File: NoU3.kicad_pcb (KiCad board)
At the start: 4 copper layers, 46 x 56 mm, 126 parts, among them J1 JST SR/SZ, J10 JST SR/SZ, J11 Screw_Terminal_01x02, J12 Screw_Terminal_01x02, J13 JST SR/SZ, J14 RFANT3216120A5T, J15 Barrel_Jack, J16 VIN, J17 JST SR/SZ, J18 GND, J2 Screw_Terminal_01x02, J3 Screw_Terminal_01x02, J4 JST SR/SZ, J5 Screw_Terminal_01x02, J6 Screw_Terminal_01x02, J7 JST SR/SZ, J8 Screw_Terminal_01x02, J9 Screw_Terminal_01x02, Q1 AO3401A, SW1 reset, SW2 boot, T1 Tab, U1 HR8833, U10 PCA9685BS, U11 Qwiic1, U15 SY8113BADC, U16 SY8113BADC, U17 USB_C_Receptacle, U18 ServoPorts_2x3, U19 ServoPorts_2x3, U2 ESP32-S3FN8, U25 MMC5983MA, U26 LSM6DSO, U3 Crystal_ESP32, U4 HR8833, U5 HR8833, U6 HR8833, U7 ServoPorts_2x3, U8 5.8 ZSPT, U9 USBLC6-2P6

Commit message: first commit for V3.4 changes
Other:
- board text added: "Alfredo NoU V3.4"
- board text removed: "Alfredo NoU V3.3"
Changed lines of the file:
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@@
 		(layer "F.SilkS")
+	)
+	(gr_line
+		(start 2.6 21.94)
+		(end 2.6 15.14)
+		(stroke
+			(width 0.25)
+			(type default)
+		)
+		(layer "F.SilkS")
+	)
+	(gr_circle
+		(center -6 5)
+		(end -9.048 5)
+		(stroke
+			(width 0.254)
+			(type solid)
+		)
+		(fill no)
+		(locked yes)
+		(layer "F.SilkS")
+	)
+	(gr_line
+		(start 8 18.6)
+		(end 3.8 18.6)
+		(stroke
+			(width 0.8)
+			(type default)
+		)
+		(layer "B.SilkS")
+	)
+	(gr_line
+		(start 8.5 18.1)
+		(end 8 18.6)
+		(stroke
+			(width 0.8)
+			(type default)
+		)
+		(layer "B.SilkS")
+	)
+	(gr_line
+		(start 9.2 18.1)
+		(end 8.5 18.1)
+		(stroke
+			(width 0.8)
+			(type default)
+		)
+		(layer "B.SilkS")
 	)
 	(gr_poly
@@
 		(fill no)
 		(locked yes)
-		(layer "F.SilkS")
-	)
-	(gr_line
-		(start 2.6 21.94)
-		(end 2.6 15.14)
-		(stroke
-			(width 0.25)
-			(type default)
-		)
-		(layer "F.SilkS")
-	)
-	(gr_circle
-		(center -6 5)
-		(end -9.048 5)
-		(stroke
-			(width 0.254)
-			(type solid)
-		)
-		(fill no)
-		(locked yes)
-		(layer "F.SilkS")
-	)
-	(gr_line
-		(start 8 18.6)
-		(end 3.8 18.6)
-		(stroke
-			(width 0.8)
-			(type default)
-		)
-		(layer "B.SilkS")
-	)
-	(gr_line
-		(start 8.5 18.1)
-		(end 8 18.6)
-		(stroke
-			(width 0.8)
-			(type default)
-		)
-		(layer "B.SilkS")
-	)
-	(gr_line
-		(start 9.2 18.1)
-		(end 8.5 18.1)
-		(stroke
-			(width 0.8)
-			(type default)
-		)
-		(layer "B.SilkS")
+		(layer "Dwgs.User")
 	)
 	(gr_arc
@@
 		)
 	)
-	(gr_text "Alfredo NoU V3.3"
+	(gr_text "Alfredo NoU V3.4"
 		(at -6.6 28.1 180)
 		(layer "B.SilkS")

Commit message: bumped version to NoU3.5
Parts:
- removed T1 (x4): Tab, PCM_kikit:Tab
- R29: value 3K -> 1K
- R30: value 1K -> 6K8
- U26: value LSM6DSO -> LSM6DSDTR
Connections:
- TP4 pad 1: Net-(U10-EXTCLK) -> M_ECLK
- U10 pad 18: /MotorSystem/MotorDriver-4/AIN1 -> /MotorSystem/MotorDriver-4/AIN2
- U10 pad 22: Net-(U10-EXTCLK) -> M_ECLK
- U2 pad 18: unconnected-(U2-GPIO13-Pad18) -> M_ECLK
- U6 pad 15: /MotorSystem/MotorDriver-4/AIN1 -> /MotorSystem/MotorDriver-4/AIN2
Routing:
- net M_ECLK: track 0.00 -> 25.7 mm, vias 0 -> 2
- net /MotorSystem/MotorDriver-4/AIN2: track 0.00 -> 7.70 mm, vias 0 -> 2
- net /MotorSystem/MotorDriver-4/AIN1: track 16.2 -> 8.55 mm, vias 4 -> 2
- net GND: track 148.8 -> 153.7 mm
- net +3V3: track 80.3 -> 83.5 mm
- net Net-(U10-EXTCLK): track 3.19 -> 0.00 mm, vias 1 -> 0
- net M_OE: track 34.6 -> 34.4 mm, vias 2 -> 3
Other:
- outline, holes or cut-outs redrawn
- board text added: "Alfredo NoU V3.5"
- board text removed: "Alfredo NoU V3.4"

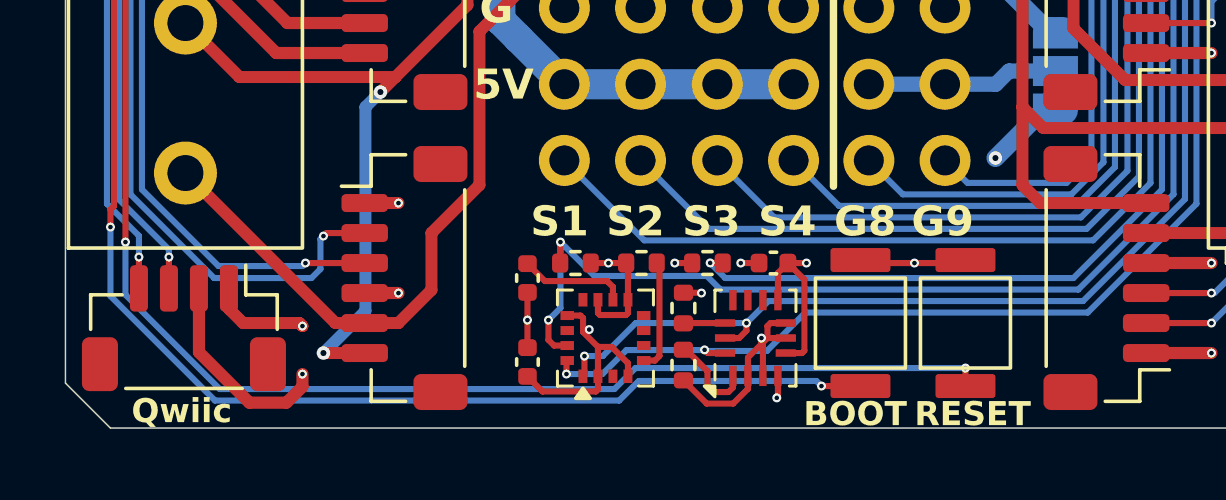
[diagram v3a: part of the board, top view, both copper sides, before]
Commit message: removed mag sensor, improved regulator resistor values
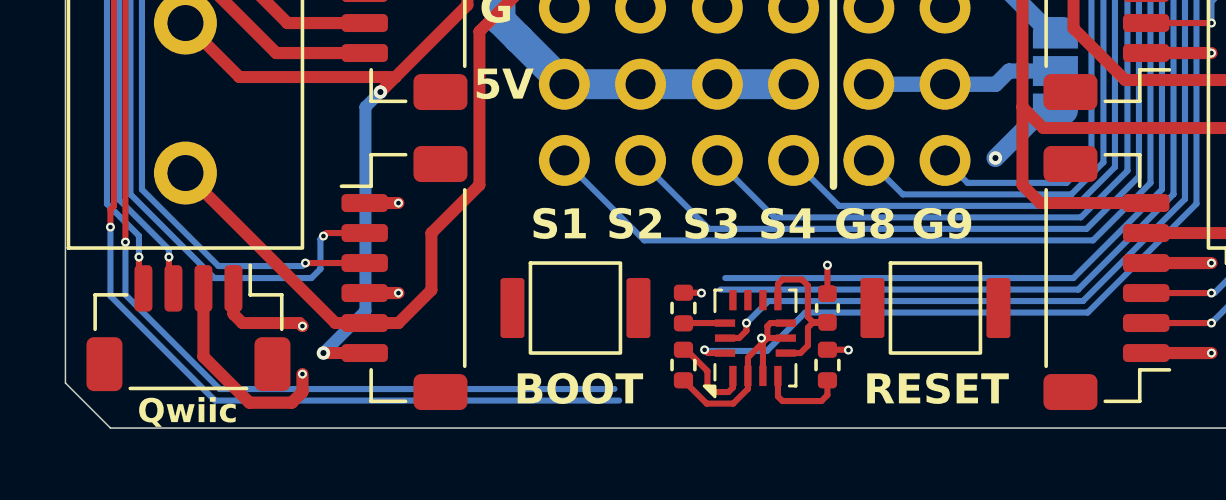
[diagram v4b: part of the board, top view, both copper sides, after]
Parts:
- removed C42: 100nF, Capacitor_SMD:C_0402_1005Metric
- removed C43: 10uF, Capacitor_SMD:C_0402_1005Metric
- removed R25, R28: 10K, Resistor_SMD:R_0402_1005Metric
- removed U25: MMC5983MA, Package_LGA:LGA-16_3x3mm_P0.5mm
- R29: value 1K -> 3K
- R30: value 6K8 -> 5K
- moved SW2 9.51 mm to (-6.00, 26.0), turned to 0 degrees
- moved R24 5.25 mm to (2.40, 27.9), turned to 90 degrees
- moved C40 2.34 mm to (2.40, 26.0), turned to 90 degrees
- moved SW1 1.12 mm to (6.00, 26.0), turned to 0 degrees
- moved U11 0.15 mm to (-18.9, 26.7)
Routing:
- net Net-(U2-CHIP_PU): track 107.5 -> 94.9 mm, vias 4 -> 3
- net SF_INT1: track 58.4 -> 47.6 mm, vias 3 -> 1
- net GND: track 153.7 -> 144.5 mm, vias 58 -> 55
- net Net-(U2-GPIO0): track 104.4 -> 96.0 mm, vias 4 -> 3
- net +3V3: track 83.5 -> 75.9 mm, vias 24 -> 22
- net SF_SCL: track 68.3 -> 61.8 mm, vias 5 -> 4
- net SF_SDA: track 72.0 -> 66.6 mm, vias 5 -> 4
- net SF_INT2: track 54.1 -> 49.8 mm, vias 3 -> 1
- net Net-(U25-SPI_SDO): track 3.72 -> 0.00 mm
- net Net-(U25-CAP): track 3.60 -> 0.00 mm

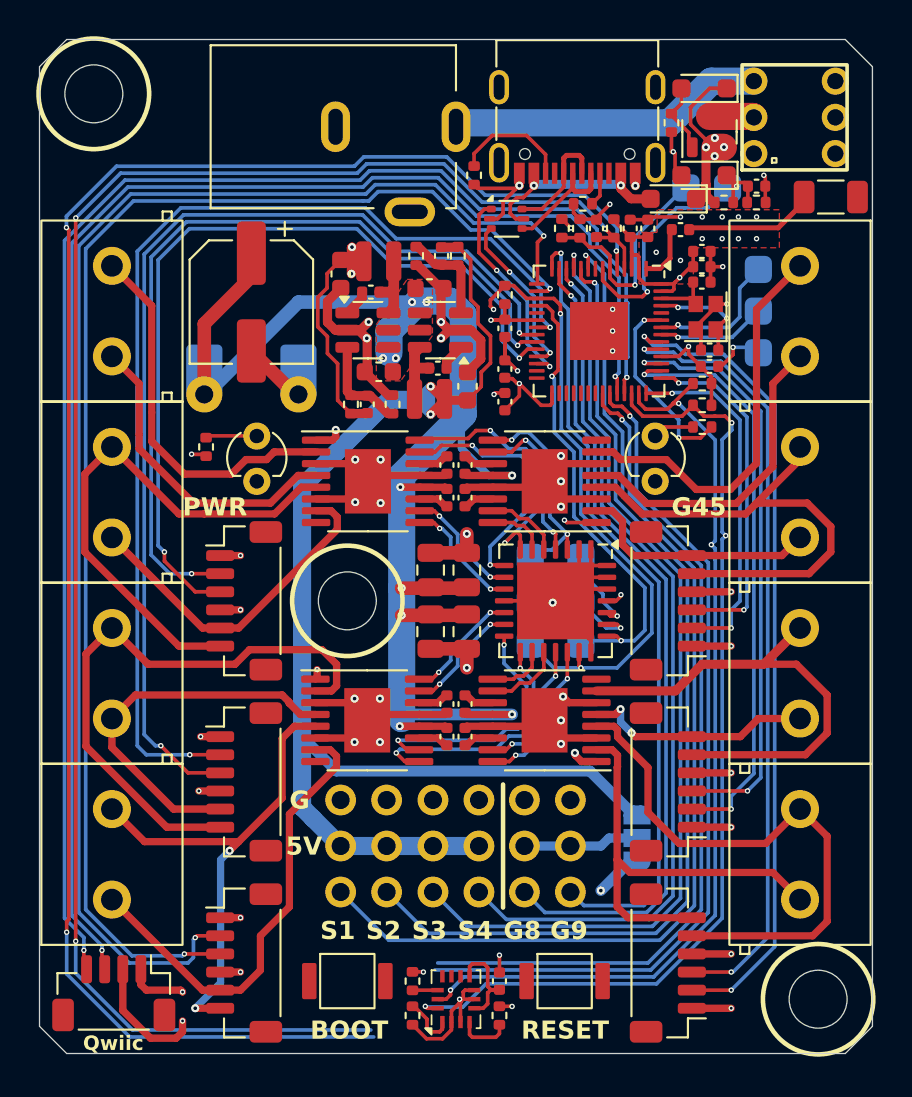
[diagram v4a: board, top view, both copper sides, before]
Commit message: added 7th encoder, 2nd 220uf cap
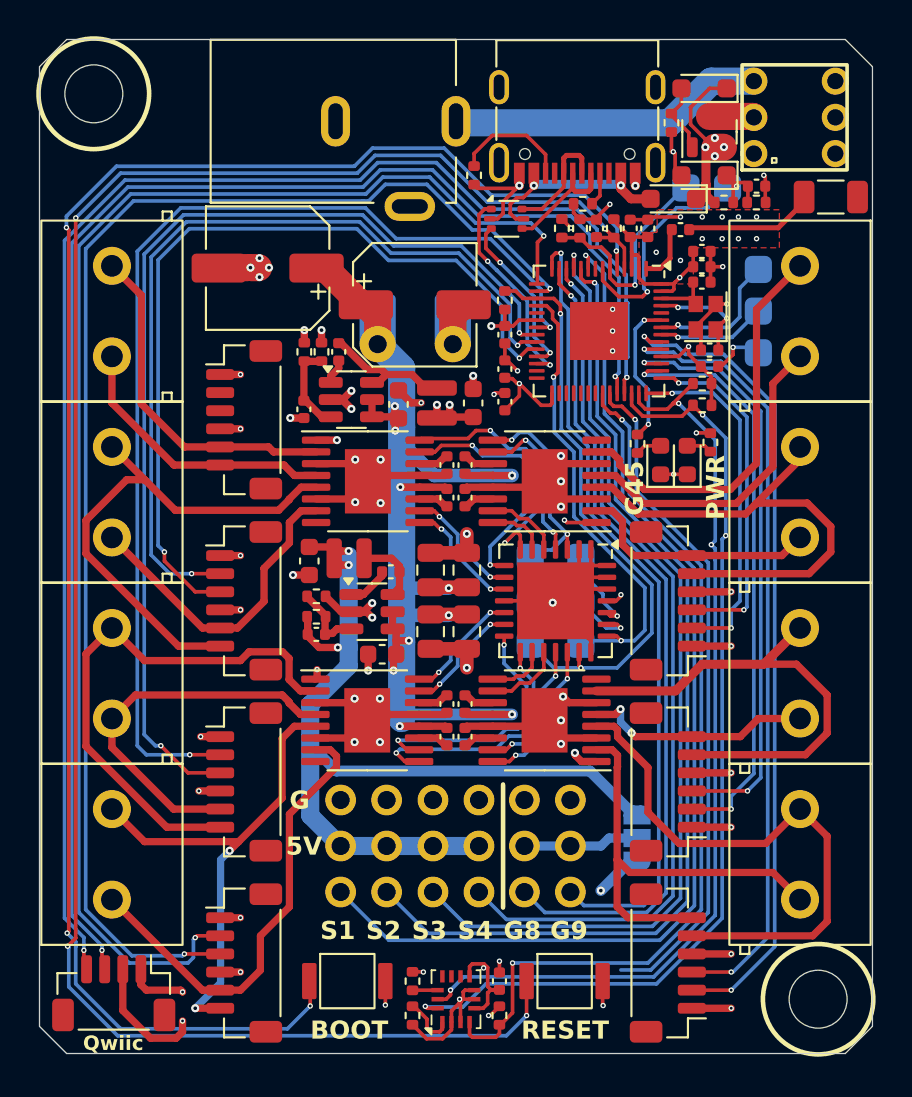
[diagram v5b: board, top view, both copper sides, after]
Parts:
- removed the ? at (-6.00, 5.00)
- added C20: 220uF, Capacitor_SMD:CP_Elec_6.3x7.7, F.Cu at (-2.27, -11.3)
- added J19: JST SR/SZ, AlfredoFootprints:JST_SH_1x06_Vertical, F.Cu at (-11.7, -5.00)
- C16: value ~ -> 220uF
- D5: value LED_blue -> LED_Blue; footprint AlfredoFootprints:LED_3mm -> LED_SMD:LED_0603_1608Metric
- D6: footprint AlfredoFootprints:LED_3mm -> LED_SMD:LED_0603_1608Metric
- R11: value 68K -> 100K
- R12: value 15K -> 22K1
- R13: value 33K -> 100K
- R14: value 4K7 -> 13K7
- moved R17 27.9 mm to (14.1, -3.75), turned to -90 degrees
- moved D5 23.8 mm to (12.8, -2.77)
- moved C33 22.0 mm to (-7.71, 6.85), turned to 0 degrees
- moved R13 21.4 mm to (-7.71, 5.88), turned to 0 degrees
- moved C23 20.4 mm to (-4.08, 7.95), turned to 180 degrees
- moved R14 19.6 mm to (-7.71, 4.75), turned to 0 degrees
- moved U16 16.0 mm to (-4.64, 5.60), turned to 0 degrees
- moved C36 13.0 mm to (-8.10, 2.80), turned to -90 degrees
- moved C29 11.5 mm to (-3.60, 3.40), turned to 0 degrees
- moved C35 10.2 mm to (0.95, -5.92), turned to 90 degrees
- moved J16 9.97 mm to (-4.33, -9.18)
- moved L2 9.86 mm to (-5.90, 2.65), turned to 180 degrees
- moved J18 8.97 mm to (-0.17, -9.18)
- moved L1 8.46 mm to (-1.05, -5.92), turned to -90 degrees
- moved R12 4.88 mm to (-7.42, -8.75)
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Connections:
- net /MotorSystem/MotorDriver-2/Aout1 renamed MD2_A1
- net /MotorSystem/MotorDriver-2/Aout2 renamed MD2_A2
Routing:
- net +5V: track 74.9 -> 51.8 mm, vias 2 -> 3
- net Net-(U2-CHIP_PU): track 94.9 -> 107.4 mm, vias 3 -> 4
- net +3V3: track 75.9 -> 65.1 mm, vias 22 -> 26
- net SF_INT1: track 47.6 -> 37.3 mm
- net VCC: track 112.9 -> 120.2 mm
- net Net-(U15-LX): track 3.77 -> 7.41 mm
- net LED_MISC: track 10.7 -> 8.03 mm
- net /MotorSystem/MotorDriver-3/Aout1: track 32.8 -> 30.2 mm
- net GND: track 144.5 -> 142.0 mm, vias 55 -> 68
- net MD2_A1: track 20.9 -> 19.0 mm
- net MD2_A2: track 17.4 -> 15.5 mm
- net M_OE: track 34.4 -> 32.5 mm, vias 3 -> 2
- net Net-(D5-A): track 2.80 -> 1.41 mm
- net Net-(U2-GPIO0): track 96.0 -> 94.7 mm, vias 3 -> 4
- net Net-(U16-FB): track 5.43 -> 4.12 mm
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- added copper zone on In2.Cu, net VCC
- removed copper zone on F.Cu, net VCC
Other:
- board text added: "5K/3K => 0.375*3.3V"
- board text removed: "1K/3K => 0.75*3.3V"

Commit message: NoU3.5s as ordered 11/6/25
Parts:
- gave numbers to parts that had none: 2
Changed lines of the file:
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@@
 		(layer "F.Cu")
 		(at -20 -23)
-		(property "Reference" ""
+		(property "Reference" "H1"
 			(at 0 0 0)
 			(layer "F.SilkS")
@@
 			)
 		)
+		(attr board_only exclude_from_pos_files exclude_from_bom dnp)
 		(pad "" np_thru_hole circle
 			(at 0 0)
@@
 		(layer "F.Cu")
 		(at 20 27)
-		(property "Reference" ""
+		(property "Reference" "H2"
 			(at 0 0 0)
 			(layer "F.SilkS")
@@
 			)
 		)
+		(attr board_only exclude_from_pos_files exclude_from_bom dnp)
 		(pad "" np_thru_hole circle
 			(at 0 0)
@@
 		(sheetname "/")
 		(sheetfile "NoU3.kicad_sch")
-		(attr smd)
+		(attr through_hole)
 		(fp_line
 			(start 4.47 4.84)

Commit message: first commit for NoU3.6
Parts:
- R29: value 3K -> 2K
- R30: value 5K -> 3K3
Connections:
- U2 pad 19: unconnected-(U2-GPIO14-Pad19) -> E7A
- U2 pad 27: unconnected-(U2-GPIO21-Pad27) -> E7B
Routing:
- net E7A: track 0.00 -> 36.9 mm, vias 0 -> 3
- net E7B: track 0.00 -> 35.1 mm, vias 0 -> 2
- net E5A: track 75.3 -> 75.8 mm
- net E3A: track 57.9 -> 58.4 mm
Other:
- board text added: "Alfredo NoU V3.6"
- board text removed: "Alfredo NoU V3.5"

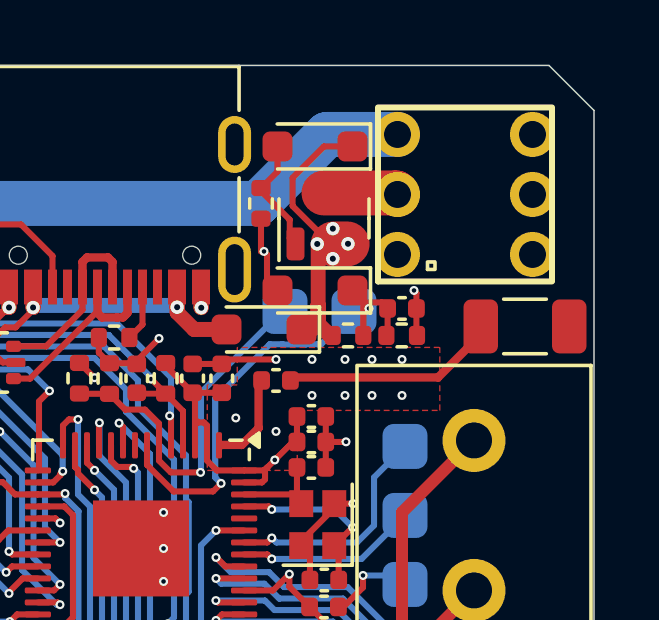
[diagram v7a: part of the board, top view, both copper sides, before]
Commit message: Update LSM6DS3TR-C part and add PCB silk circle
Changed the schematic part value, datasheet, and LCSC code from LSM6DSDTR to LSM6DS3TR-C. Added a new circle to the F.SilkS layer in the PCB. Removed the auto-saved files reference.
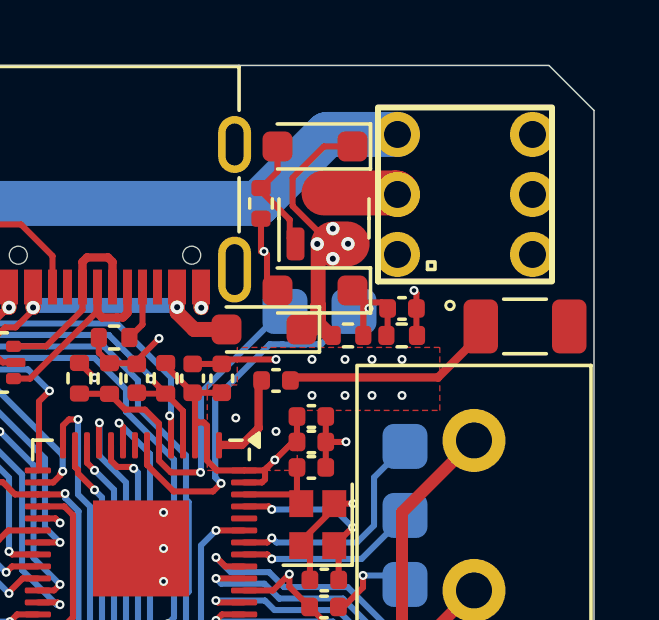
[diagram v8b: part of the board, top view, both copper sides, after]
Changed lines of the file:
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@@
+	)
+	(gr_circle
+		(center 18.2 -18)
+		(end 18.3 -17.9)
+		(stroke
+			(width 0.1)
+			(type default)
+		)
+		(fill no)
+		(layer "F.SilkS")
 	)
 	(gr_circle
